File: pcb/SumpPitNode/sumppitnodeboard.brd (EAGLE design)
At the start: 63.2 x 64.8 mm, 37 parts, among them IC1 7805T

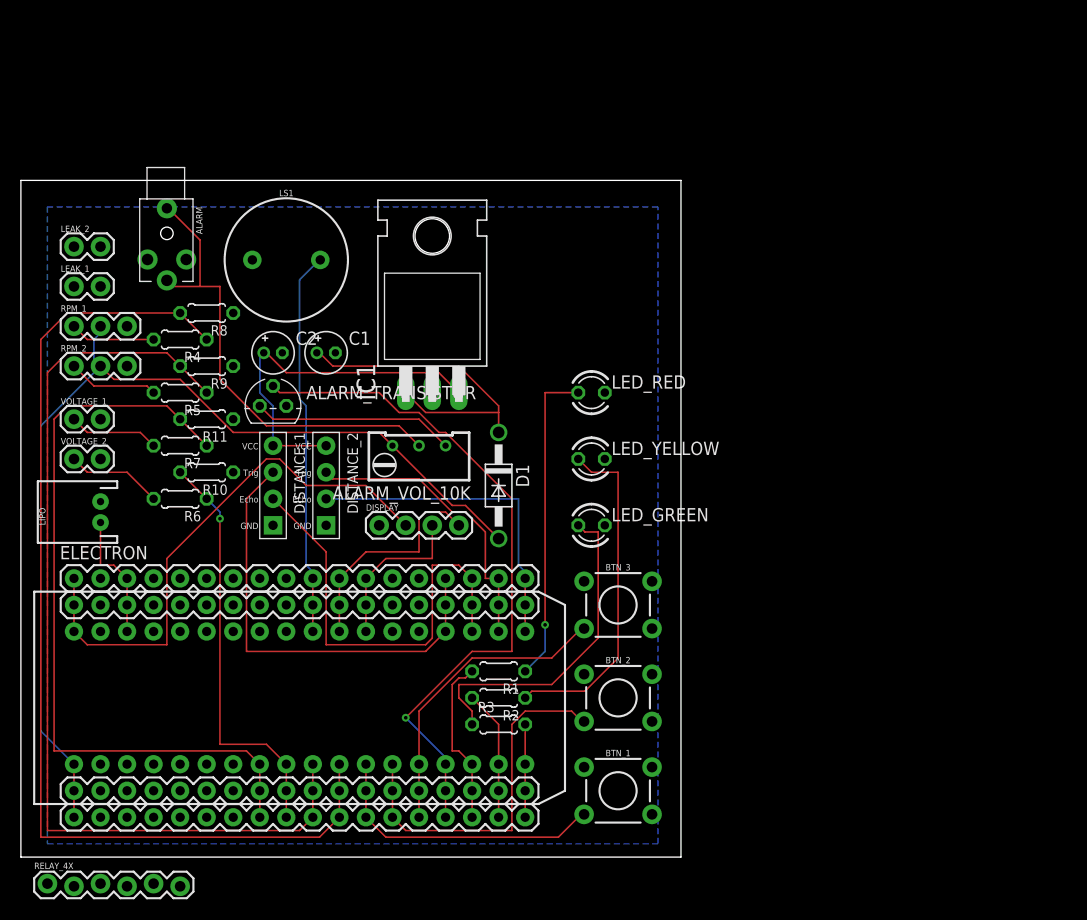
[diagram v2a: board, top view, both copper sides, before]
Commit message: Place 4relay.
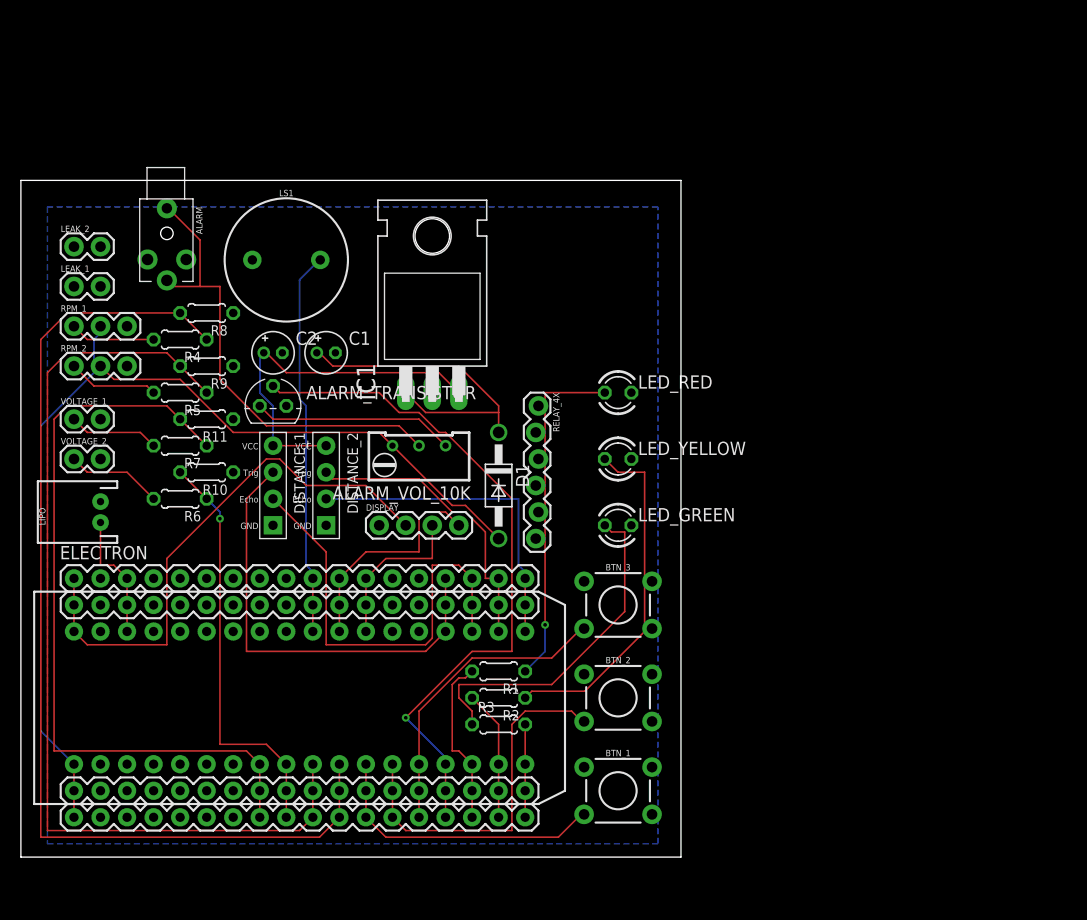
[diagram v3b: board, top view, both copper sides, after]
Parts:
- moved RELAY_4X 65.6 mm to (49.5, 43.2), turned to 270 degrees
- moved LED_GREEN 2.54 mm to (57.1, 31.8)
- moved LED_RED 2.54 mm to (57.1, 44.5)
- moved LED_YELLOW 2.54 mm to (57.1, 38.1)
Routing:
- net N$4: track 30.6 -> 33.2 mm
- net N$21: track 31.8 -> 32.9 mm
- net N$20: track 32.6 -> 33.6 mm
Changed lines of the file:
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@@
 <element name="LEAK_1" library="SparkFun-Connectors" library_urn="urn:adsk.eagle:library:513" package="1X02" package3d_urn="urn:adsk.eagle:package:38039/1" value="" x="5.08" y="54.61"/>
 <element name="LEAK_2" library="SparkFun-Connectors" library_urn="urn:adsk.eagle:library:513" package="1X02" package3d_urn="urn:adsk.eagle:package:38039/1" value="" x="5.08" y="58.42"/>
-<element name="LED_GREEN" library="led" library_urn="urn:adsk.eagle:library:259" package="LED3MM" package3d_urn="urn:adsk.eagle:package:15797/1" value="" x="54.61" y="31.75"/>
-<element name="LED_RED" library="led" library_urn="urn:adsk.eagle:library:259" package="LED3MM" package3d_urn="urn:adsk.eagle:package:15797/1" value="" x="54.61" y="44.45"/>
-<element name="LED_YELLOW" library="led" library_urn="urn:adsk.eagle:library:259" package="LED3MM" package3d_urn="urn:adsk.eagle:package:15797/1" value="" x="54.61" y="38.1"/>
+<element name="LED_GREEN" library="led" library_urn="urn:adsk.eagle:library:259" package="LED3MM" package3d_urn="urn:adsk.eagle:package:15797/1" value="" x="57.15" y="31.75"/>
+<element name="LED_RED" library="led" library_urn="urn:adsk.eagle:library:259" package="LED3MM" package3d_urn="urn:adsk.eagle:package:15797/1" value="" x="57.15" y="44.45"/>
+<element name="LED_YELLOW" library="led" library_urn="urn:adsk.eagle:library:259" package="LED3MM" package3d_urn="urn:adsk.eagle:package:15797/1" value="" x="57.15" y="38.1"/>
 <element name="LIPO" library="SparkFun-Connectors" library_urn="urn:adsk.eagle:library:513" package="JST-2-PTH" package3d_urn="urn:adsk.eagle:package:38053/1" value="" x="7.62" y="33.02" rot="R90">
 <attribute name="PROD_ID" value="CONN-09863" x="7.62" y="33.02" size="1.778" layer="27" rot="R90" display="off"/>
@@
 <element name="VOLTAGE_2" library="SparkFun-Connectors" library_urn="urn:adsk.eagle:library:513" package="1X02" package3d_urn="urn:adsk.eagle:package:38039/1" value="" x="5.08" y="38.1"/>
 <element name="R11" library="resistor" library_urn="urn:adsk.eagle:library:348" package="0204/5" package3d_urn="urn:adsk.eagle:package:25955/1" value="" x="17.78" y="41.91" rot="R180"/>
-<element name="RELAY_4X" library="SparkFun-Connectors" package="1X06_LOCK" value="" x="2.54" y="-2.54"/>
+<element name="RELAY_4X" library="SparkFun-Connectors" package="1X06_LOCK" value="" x="49.53" y="43.18" rot="R270"/>
 </elements>
 <signals>
@@
 </polygon>
 <contactref element="RELAY_4X" pad="6"/>
-<wire x1="55.88" y1="38.1" x2="55.88" y2="44.45" width="0" layer="19" extent="1-1"/>
-<wire x1="55.88" y1="31.75" x2="55.88" y2="38.1" width="0" layer="19" extent="1-1"/>
-<wire x1="53.8988" y1="26.3906" x2="55.88" y2="31.75" width="0" layer="19" extent="1-1"/>
+<wire x1="58.42" y1="38.1" x2="58.42" y2="44.45" width="0" layer="19" extent="1-1"/>
+<wire x1="58.42" y1="31.75" x2="58.42" y2="38.1" width="0" layer="19" extent="1-1"/>
+<wire x1="53.8988" y1="26.3906" x2="58.42" y2="31.75" width="0" layer="19" extent="1-1"/>
 <wire x1="53.8988" y1="17.5006" x2="53.8988" y2="26.3906" width="0" layer="19" extent="1-1"/>
 <wire x1="53.8988" y1="8.6106" x2="53.8988" y2="17.5006" width="0" layer="19" extent="1-1"/>
-<wire x1="39.37" y1="44.45" x2="55.88" y2="44.45" width="0" layer="19" extent="1-1"/>
+<wire x1="39.37" y1="44.45" x2="58.42" y2="44.45" width="0" layer="19" extent="1-1"/>
 <wire x1="30.099" y1="48.26" x2="39.37" y2="44.45" width="0" layer="19" extent="1-1"/>
 <wire x1="25.019" y1="48.26" x2="30.099" y2="48.26" width="0" layer="19" extent="1-1"/>
@@
 <wire x1="7.62" y1="6.35" x2="7.62" y2="8.89" width="0" layer="19" extent="1-1"/>
 <wire x1="7.62" y1="3.81" x2="7.62" y2="6.35" width="0" layer="19" extent="1-1"/>
-<wire x1="15.24" y1="-2.794" x2="7.62" y2="3.81" width="0" layer="19" extent="1-1"/>
+<wire x1="49.276" y1="30.48" x2="7.62" y2="3.81" width="0" layer="19" extent="1-1"/>
 </signal>
 <signal name="N$1">
@@
 <wire x1="50.165" y1="22.225" x2="50.165" y2="19.685" width="0.1524" layer="16"/>
 <wire x1="50.165" y1="44.45" x2="50.165" y2="22.225" width="0.1524" layer="1"/>
-<wire x1="53.34" y1="44.45" x2="50.165" y2="44.45" width="0.1524" layer="1"/>
+<wire x1="55.88" y1="44.45" x2="50.165" y2="44.45" width="0.1524" layer="1"/>
 <via x="50.165" y="22.225" extent="1-16" drill="0.35"/>
 </signal>
@@
 <wire x1="48.895" y1="15.875" x2="48.26" y2="15.24" width="0.1524" layer="1"/>
 <wire x1="53.975" y1="15.875" x2="48.895" y2="15.875" width="0.1524" layer="1"/>
-<wire x1="57.15" y1="19.05" x2="53.975" y2="15.875" width="0.1524" layer="1"/>
-<wire x1="57.15" y1="36.83" x2="57.15" y2="19.05" width="0.1524" layer="1"/>
-<wire x1="54.61" y1="36.83" x2="57.15" y2="36.83" width="0.1524" layer="1"/>
-<wire x1="53.34" y1="38.1" x2="54.61" y2="36.83" width="0.1524" layer="1"/>
+<wire x1="59.69" y1="21.59" x2="53.975" y2="15.875" width="0.1524" layer="1"/>
+<wire x1="59.69" y1="36.83" x2="59.69" y2="21.59" width="0.1524" layer="1"/>
+<wire x1="57.15" y1="36.83" x2="59.69" y2="36.83" width="0.1524" layer="1"/>
+<wire x1="55.88" y1="38.1" x2="57.15" y2="36.83" width="0.1524" layer="1"/>
 </signal>
 <signal name="N$21">
@@
 <wire x1="41.91" y1="16.51" x2="41.91" y2="15.24" width="0.1524" layer="1"/>
 <wire x1="50.8" y1="16.51" x2="41.91" y2="16.51" width="0.1524" layer="1"/>
-<wire x1="55.245" y1="20.955" x2="50.8" y2="16.51" width="0.1524" layer="1"/>
-<wire x1="55.245" y1="31.115" x2="55.245" y2="20.955" width="0.1524" layer="1"/>
-<wire x1="53.975" y1="31.115" x2="55.245" y2="31.115" width="0.1524" layer="1"/>
-<wire x1="53.34" y1="31.75" x2="53.975" y2="31.115" width="0.1524" layer="1"/>
+<wire x1="57.785" y1="23.495" x2="50.8" y2="16.51" width="0.1524" layer="1"/>
+<wire x1="57.785" y1="31.115" x2="57.785" y2="23.495" width="0.1524" layer="1"/>
+<wire x1="56.515" y1="31.115" x2="57.785" y2="31.115" width="0.1524" layer="1"/>
+<wire x1="55.88" y1="31.75" x2="56.515" y2="31.115" width="0.1524" layer="1"/>
 </signal>
 <signal name="N$22">
@@
 <wire x1="22.86" y1="48.26" x2="23.241" y2="48.26" width="0.1524" layer="16"/>
 <contactref element="RELAY_4X" pad="5"/>
-<wire x1="12.7" y1="-2.54" x2="24.13" y2="39.37" width="0" layer="19" extent="1-1"/>
+<wire x1="49.53" y1="33.02" x2="24.13" y2="39.37" width="0" layer="19" extent="1-1"/>
 </signal>
 <signal name="N$34">
@@
 <wire x1="25.4" y1="24.13" x2="25.4" y2="26.67" width="0" layer="19" extent="1-1"/>
 <wire x1="25.4" y1="21.59" x2="25.4" y2="24.13" width="0" layer="19" extent="1-1"/>
-<wire x1="10.16" y1="-2.794" x2="25.4" y2="21.59" width="0" layer="19" extent="1-1"/>
+<wire x1="49.276" y1="35.56" x2="25.4" y2="21.59" width="0" layer="19" extent="1-1"/>
 </signal>
 <signal name="N$35">
@@
 <wire x1="22.86" y1="24.13" x2="22.86" y2="26.67" width="0" layer="19" extent="1-1"/>
 <wire x1="22.86" y1="21.59" x2="22.86" y2="24.13" width="0" layer="19" extent="1-1"/>
-<wire x1="7.62" y1="-2.54" x2="22.86" y2="21.59" width="0" layer="19" extent="1-1"/>
+<wire x1="49.53" y1="38.1" x2="22.86" y2="21.59" width="0" layer="19" extent="1-1"/>
 </signal>
 <signal name="N$36">
@@
 <wire x1="20.32" y1="24.13" x2="20.32" y2="26.67" width="0" layer="19" extent="1-1"/>
 <wire x1="20.32" y1="21.59" x2="20.32" y2="24.13" width="0" layer="19" extent="1-1"/>
-<wire x1="5.08" y1="-2.794" x2="20.32" y2="21.59" width="0" layer="19" extent="1-1"/>
+<wire x1="49.276" y1="40.64" x2="20.32" y2="21.59" width="0" layer="19" extent="1-1"/>
 </signal>
 <signal name="N$37">
@@
 <wire x1="17.78" y1="24.13" x2="17.78" y2="26.67" width="0" layer="19" extent="1-1"/>
 <wire x1="17.78" y1="21.59" x2="17.78" y2="24.13" width="0" layer="19" extent="1-1"/>
-<wire x1="2.54" y1="-2.54" x2="17.78" y2="21.59" width="0" layer="19" extent="1-1"/>
+<wire x1="49.53" y1="43.18" x2="17.78" y2="21.59" width="0" layer="19" extent="1-1"/>
 </signal>
 </signals>

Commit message: Add power, update routing.
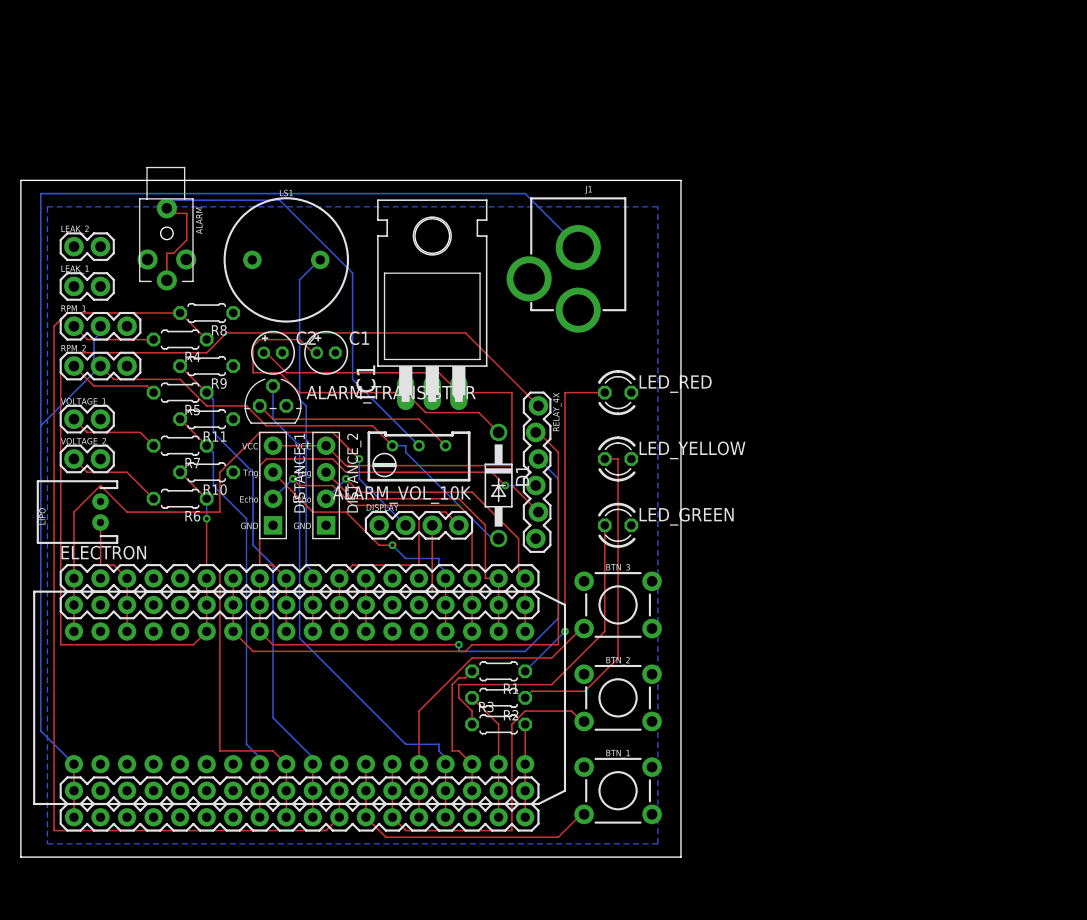
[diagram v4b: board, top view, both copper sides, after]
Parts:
- added J1: POWER_JACK, SparkFun-Connectors:POWER_JACK_PTH
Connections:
- net GND: now also J1.PWR
- net VCC_1: now also J1.GND
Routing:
- net N$37: track 0.00 -> 96.5 mm
- net VCC_1: track 97.4 -> 172.7 mm
- net N$36: track 0.00 -> 58.6 mm
- net N$35: track 0.00 -> 52.2 mm, vias 0 -> 1
- net N$34: track 0.00 -> 45.4 mm, vias 0 -> 1
- net N$29: track 92.4 -> 48.4 mm
- net N$31: track 73.8 -> 41.3 mm
- net N$33: track 35.1 -> 61.5 mm
- net N$17: track 43.1 -> 26.5 mm, vias 0 -> 1
- net N$3: track 65.8 -> 50.0 mm, vias 1 -> 0
- net N$13: track 42.9 -> 32.2 mm, vias 0 -> 1
- net N$1: track 45.4 -> 50.6 mm
- net N$18: track 31.7 -> 35.3 mm
- net N$14: track 52.2 -> 55.5 mm, vias 0 -> 1
- net N$20: track 33.6 -> 30.8 mm
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
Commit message: Connect leak sensors.
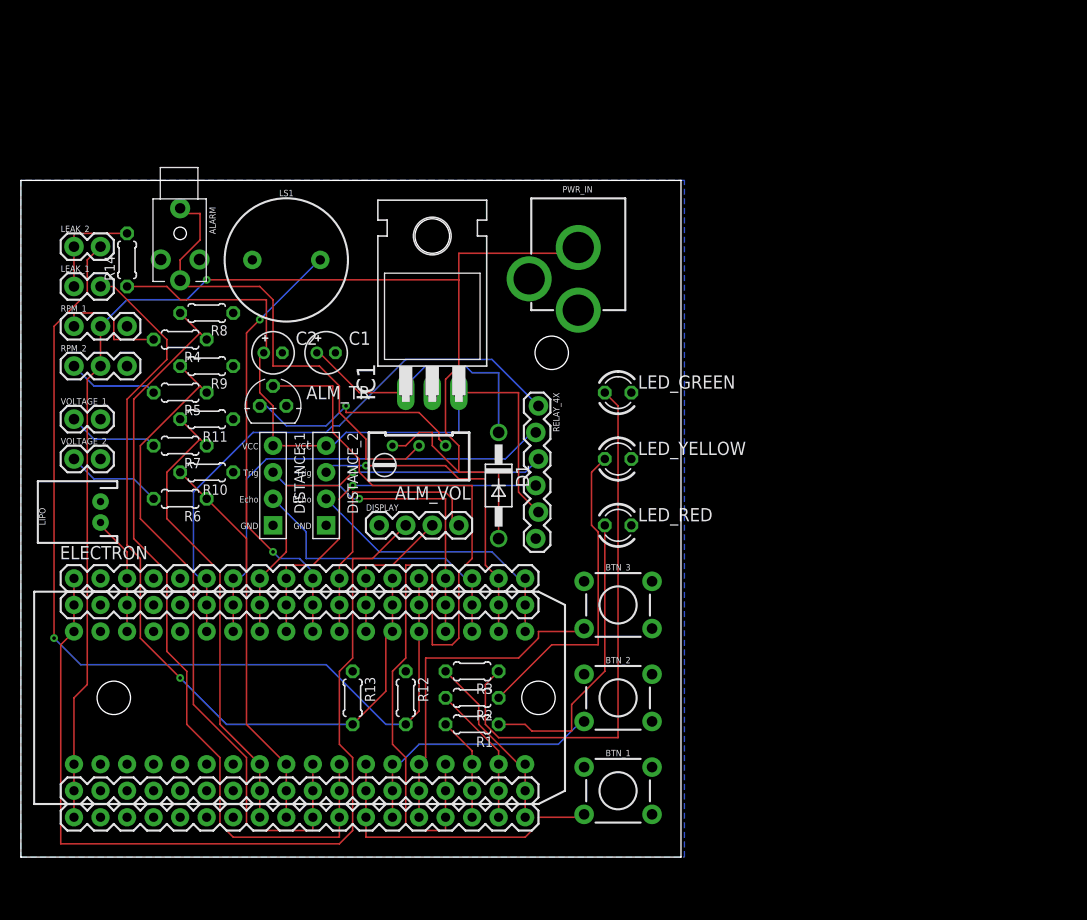
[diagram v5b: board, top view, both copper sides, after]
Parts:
- added R12, R13: 5M, resistor:0204/5
- added R14: 100K, resistor:0204/5
- ALM_VOL: value (none) -> 10k
- moved LED_GREEN 12.7 mm to (57.1, 44.5)
- moved LED_RED 12.7 mm to (57.1, 31.8)
- moved R1 5.68 mm to (43.2, 12.7)
- moved R3 5.68 mm to (43.2, 17.8), turned to 180 degrees
- moved R2 2.54 mm to (43.2, 15.2)
- moved ALARM 1.27 mm to (15.2, 59.7)
- renumbered ALARM_TRANSISTOR to ALM_TR, ALARM_VOL_10K to ALM_VOL, J1 to PWR_IN
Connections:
- new net N$23: ELECTRON.103, ELECTRON.67, ELECTRON.C5, LEAK_1.2, R13.2
- new net N$32: ELECTRON.104, ELECTRON.68, ELECTRON.C4, LEAK_2.2, R12.2
- new net N$38: LEAK_1.1, LEAK_2.1, R14.2
- net GND: now also R12.1, R13.1
- net N$33: now also R14.1
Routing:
- net N$32: track 0.00 -> 90.9 mm, vias 0 -> 1
- net N$23: track 0.00 -> 78.4 mm, vias 0 -> 1
- net N$37: track 96.5 -> 54.4 mm
- net N$3: track 50.0 -> 90.3 mm
- net VCC_1: track 172.7 -> 137.5 mm, vias 0 -> 1
- net N$14: track 55.5 -> 87.9 mm, vias 1 -> 0
- net N$21: track 30.6 -> 52.4 mm
- net N$28: track 97.4 -> 75.6 mm
- net N$29: track 48.4 -> 65.0 mm
- net N$36: track 58.6 -> 45.0 mm
- net N$35: track 52.2 -> 40.2 mm
- net N$38: track 0.00 -> 10.2 mm
- net N$9: track 35.0 -> 25.1 mm
- net N$34: track 45.4 -> 35.6 mm
- net N$18: track 35.3 -> 26.4 mm
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
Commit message: Reconnect leak sensors without pulldown.
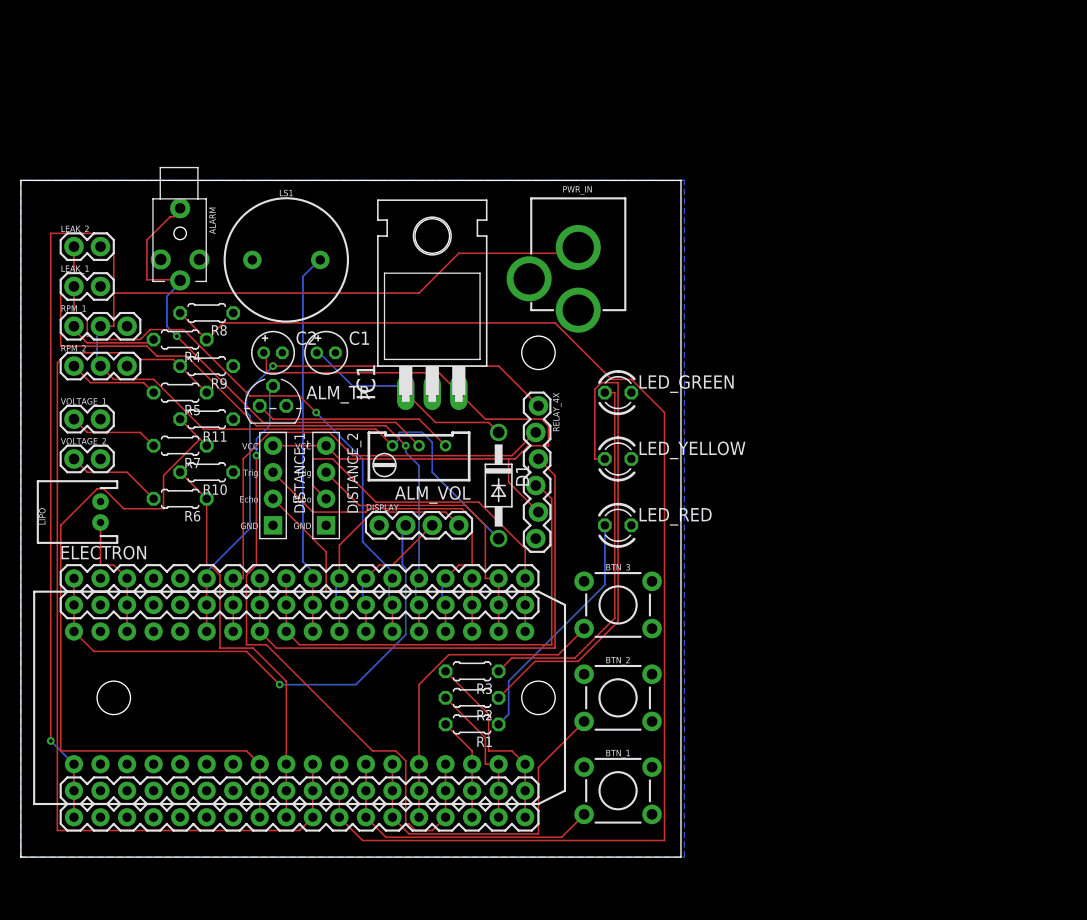
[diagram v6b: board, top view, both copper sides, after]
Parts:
- removed R12, R13: 5M, resistor:0204/5
- removed R14: 100K, resistor:0204/5
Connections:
- net N$14 renamed 3V3
- net N$28 renamed PIN_RPM_1
- net N$29 renamed PIN_RPM_2
- net N$30 renamed PIN_VOLT_2
- net N$31 renamed PIN_VOLT_1
- removed net N$38: LEAK_1.1, LEAK_2.1, R14.2
- net GND: now also LEAK_1.2, LEAK_2.2; no longer R12.1, R13.1
- net N$23: now also LEAK_1.1; no longer LEAK_1.2, R13.2
- net N$32: now also LEAK_2.1; no longer LEAK_2.2, R12.2
- net N$33: no longer R14.1
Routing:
- net PIN_RPM_1: track 75.6 -> 129.7 mm
- net 3V3: track 87.9 -> 51.6 mm, vias 0 -> 1
- net VCC_1: track 137.5 -> 171.1 mm
- net N$3: track 90.3 -> 61.4 mm, vias 0 -> 1
- net PIN_RPM_2: track 65.0 -> 91.1 mm
- net PIN_VOLT_1: track 44.8 -> 70.0 mm
- net N$32: track 90.9 -> 66.0 mm
- net N$23: track 78.4 -> 55.6 mm
- net N$20: track 30.2 -> 47.4 mm
- net N$21: track 52.4 -> 35.8 mm
- net N$35: track 40.2 -> 52.8 mm, vias 1 -> 0
- net N$34: track 35.6 -> 47.0 mm, vias 1 -> 0
- net N$38: track 10.2 -> 0.00 mm
- net N$15: track 27.3 -> 36.1 mm
- net N$9: track 25.1 -> 32.3 mm
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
